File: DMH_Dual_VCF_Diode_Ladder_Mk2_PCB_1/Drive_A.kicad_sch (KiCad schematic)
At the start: 25 parts, among them J17 Conn_01x06_PinHeader, Q5 BC548, Q6 BC548, U9 TL074

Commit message: Added trim pot functions to silkscreen
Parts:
- RV26: Function (none) -> Drive A VCA Center
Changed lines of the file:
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@@
 		(on_board yes)
 		(dnp no)
-		(fields_autoplaced yes)
 		(property "Reference" "RV26"
 			(at 224.79 100.3299 0)
@@
 			)
 		)
+		(property "Function" "Drive A VCA Center"
+			(at 239.268 101.6 0)
+			(effects
+				(font
+					(size 1.27 1.27)
+					(thickness 0.254)
+					(bold yes)
+					(italic yes)
+				)
+			)
+		)

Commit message: Adjusted pin header connections
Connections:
- net Drive CV Input: now also J17.2 (Pin_2); no longer J17.1 (Pin_1)
- net at R113.1, RV27.2: now also J17.1 (Pin_1); no longer J17.3 (Pin_3)
- net at RV25.2, U9.12 (+): now also J17.3 (Pin_3); no longer J17.2 (Pin_2)
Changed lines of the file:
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@@
 		(lib_id "SynthStuff:Conn_01x06_PinHeader")
 		(at 63.5 81.28 270)
-		(unit 1)
+		(unit 2)
 		(exclude_from_sim no)
 		(in_bom yes)
@@
 				(path "/58f4306d-5387-4983-bb08-41a2313fd315/76f3ab41-888d-43b6-843a-2a995f9c890b"
 					(reference "J17")
-					(unit 1)
+					(unit 2)
 				)
 			)
@@
 		(lib_id "SynthStuff:Conn_01x06_PinHeader")
 		(at 76.2 100.33 90)
-		(unit 2)
+		(unit 3)
 		(exclude_from_sim no)
 		(in_bom yes)
@@
 				(path "/58f4306d-5387-4983-bb08-41a2313fd315/76f3ab41-888d-43b6-843a-2a995f9c890b"
 					(reference "J17")
-					(unit 2)
+					(unit 3)
 				)
 			)
@@
 		(lib_id "SynthStuff:Conn_01x06_PinHeader")
 		(at 110.49 129.54 90)
-		(unit 3)
+		(unit 1)
 		(exclude_from_sim no)
 		(in_bom yes)
@@
 				(path "/58f4306d-5387-4983-bb08-41a2313fd315/76f3ab41-888d-43b6-843a-2a995f9c890b"
 					(reference "J17")
-					(unit 3)
-				)
-			)
+					(unit 1)
+				)
+			)

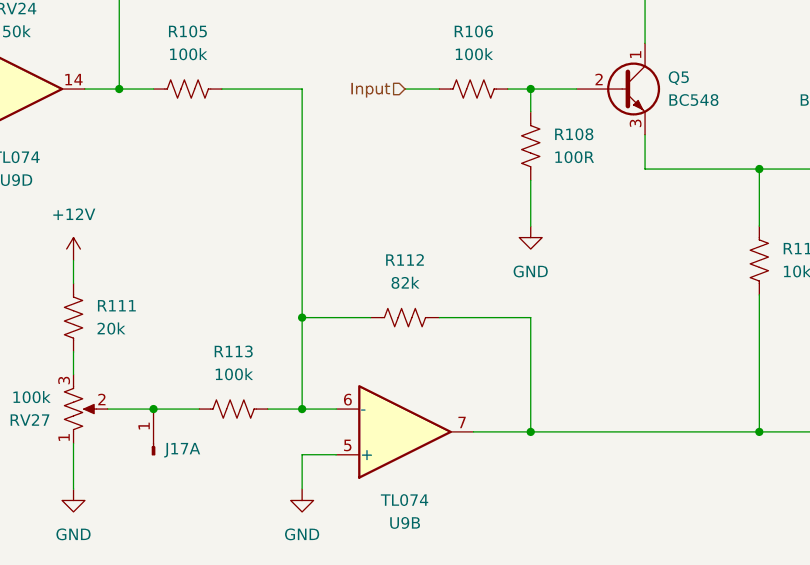
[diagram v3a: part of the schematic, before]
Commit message: Changed VCA CV summing stage feedback to 100k
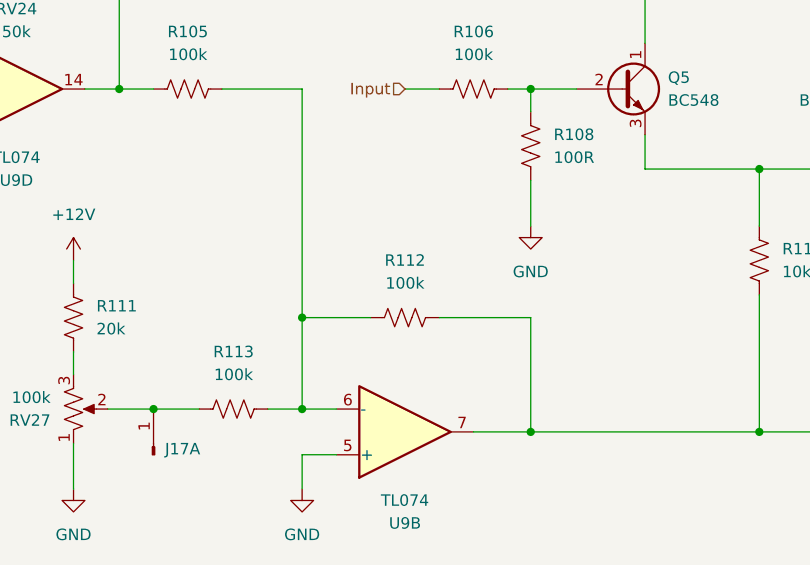
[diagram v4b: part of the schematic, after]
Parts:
- R112: value 82k -> 100k
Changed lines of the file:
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@@
 			)
 		)
-		(property "Value" "82k"
+		(property "Value" "100k"
 			(at 138.43 110.49 90)
 			(effects

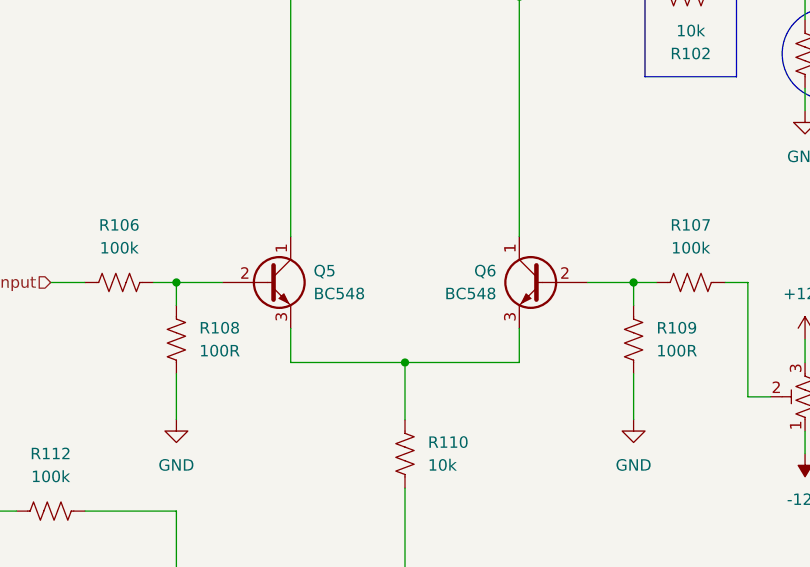
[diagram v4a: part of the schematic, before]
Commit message: Adding buffered input to CV3 - in progress
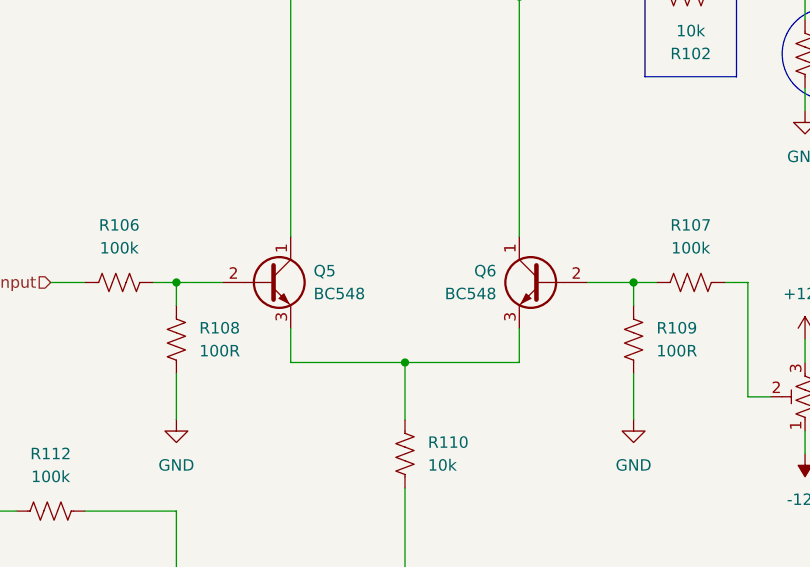
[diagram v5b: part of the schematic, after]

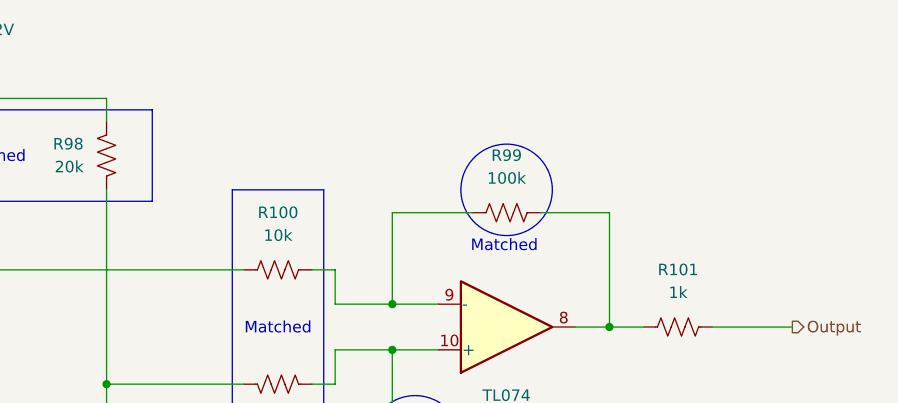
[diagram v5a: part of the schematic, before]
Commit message: Updated schematic during validation
- Changed Resonance B VCA gain resistors to 2k2
- Added range limiting resistors to all Cutoff pots
- Moved 48x gain to non-inverting opamp stage in Core Circuit to allow for Resonance voltage control.
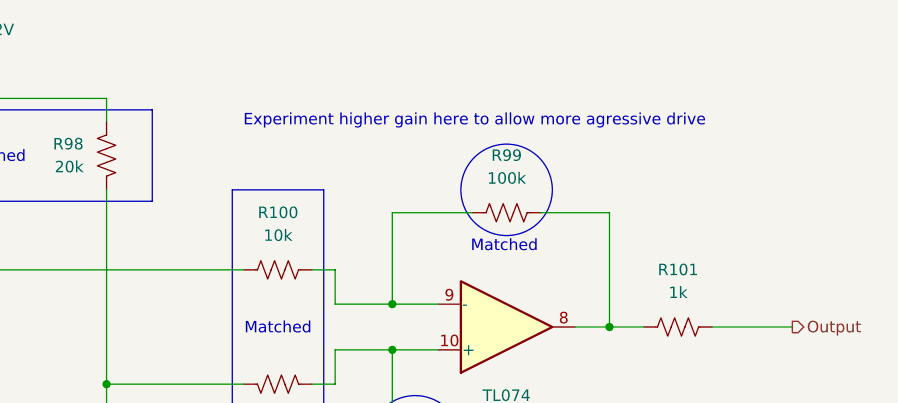
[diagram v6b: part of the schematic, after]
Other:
- note added: "Experiment higher gain here to allow more agressive drive"
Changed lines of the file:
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@@
+		)
+	)
+	(text "Experiment higher gain here to allow more agressive drive"
+		(exclude_from_sim no)
+		(at 231.394 27.94 0)
+		(effects
+			(font
+				(size 1.27 1.27)
+			)
 		)
 	)

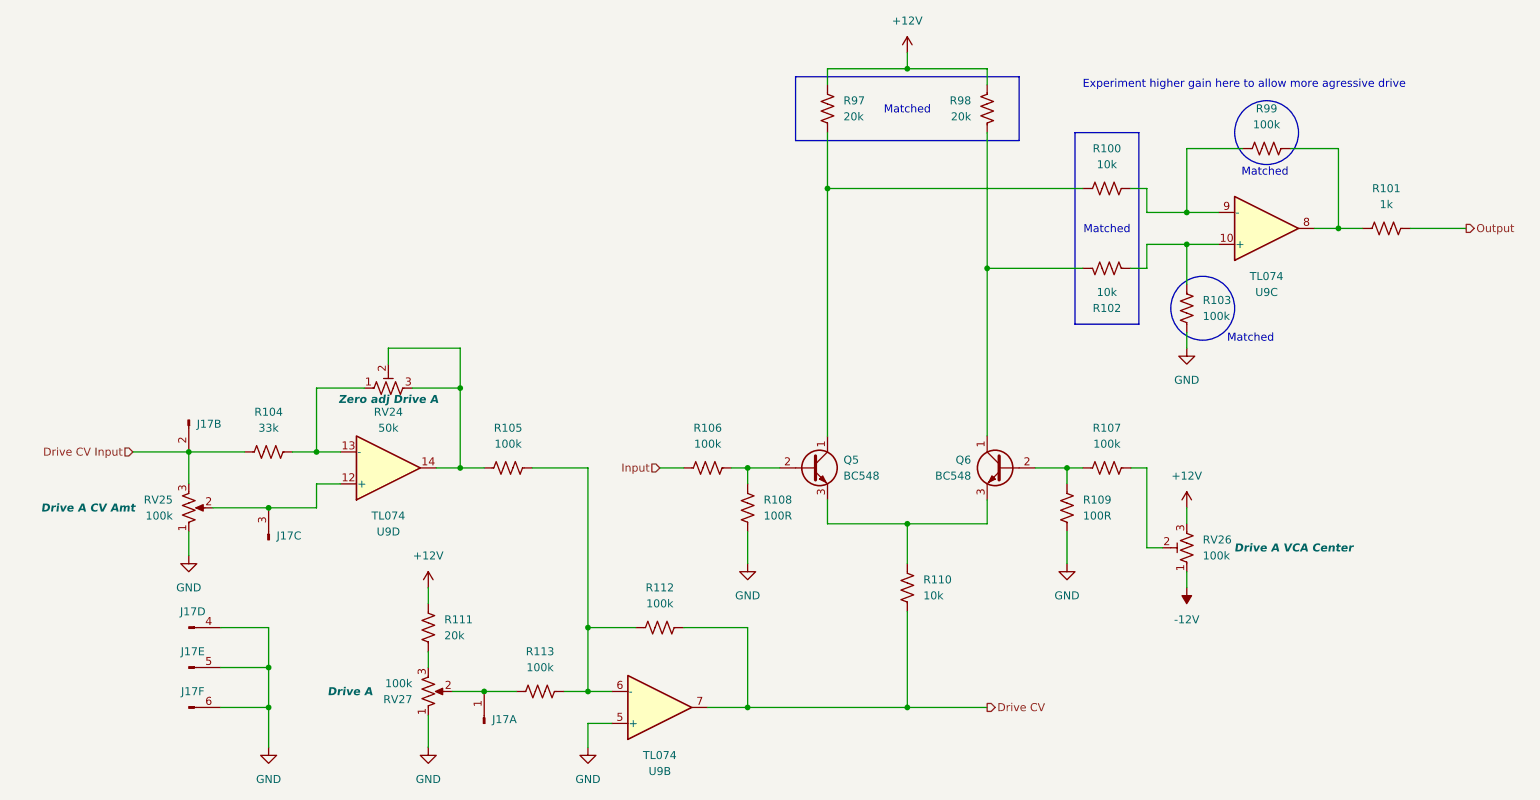
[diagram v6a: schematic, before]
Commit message: Updated various resistor values
... and deleted all VCAs output 1k resistors
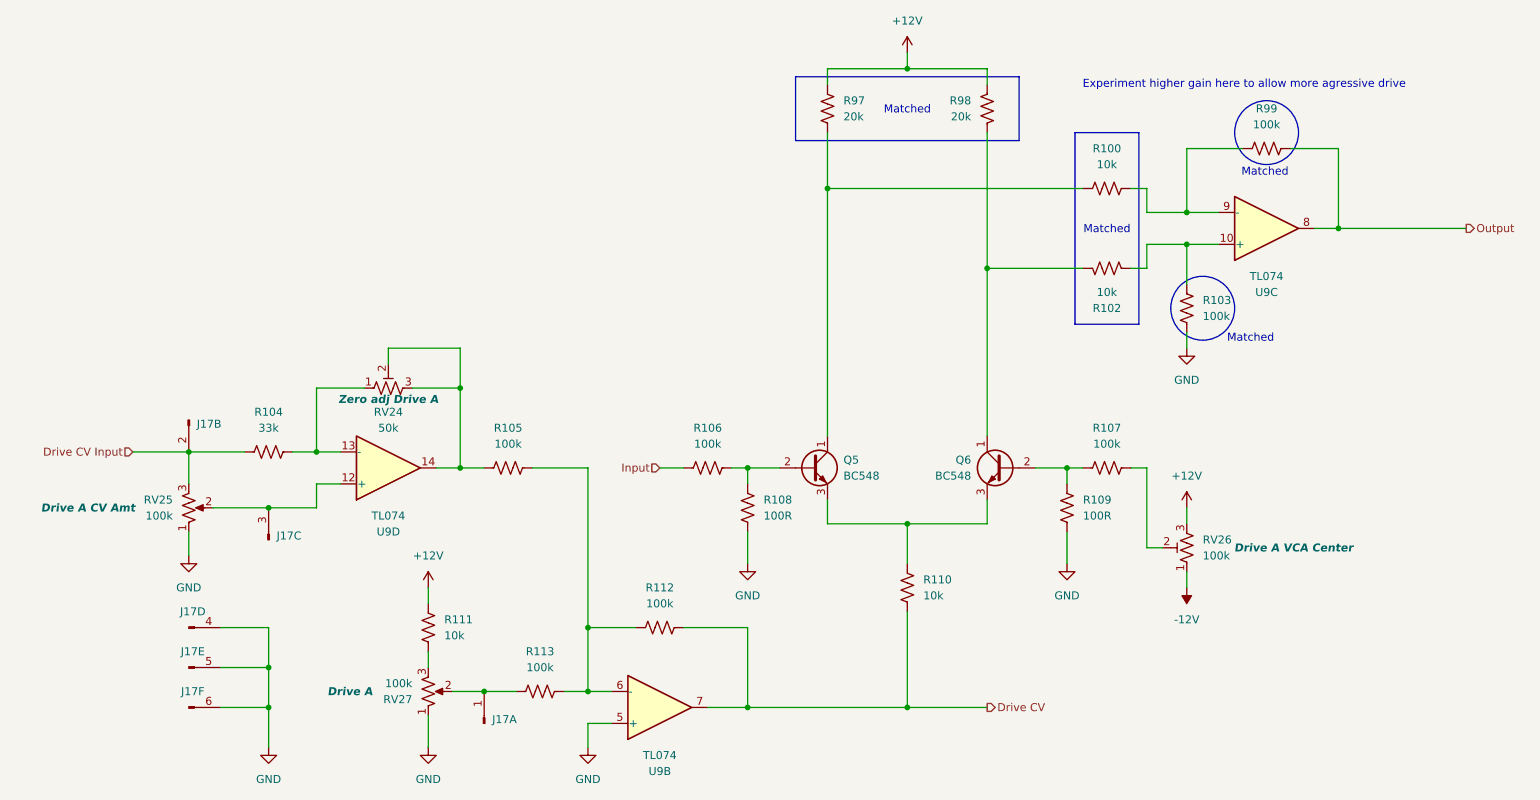
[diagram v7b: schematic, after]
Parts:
- removed R101: 1k, Resistor_THT:R_Axial_DIN0207_L6.3mm_D2.5mm_P7.62mm_Horizontal, symbol Device:R_US
- R111: value 20k -> 10k
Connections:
- net Output: now also R99.1, U9.8
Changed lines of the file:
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@@
 	(wire
 		(pts
-			(xy 257.81 50.8) (xy 266.7 50.8)
-		)
-		(stroke
-			(width 0)
-			(type default)
-		)
-	)
-	(wire
-		(pts
 			(xy 101.6 107.95) (xy 101.6 110.49)
 		)
@@
 	(wire
 		(pts
-			(xy 246.38 50.8) (xy 250.19 50.8)
+			(xy 246.38 50.8) (xy 266.7 50.8)
 		)
 		(stroke
@@
 	(symbol
 		(lib_id "Device:R_US")
-		(at 254 50.8 270)
-		(unit 1)
-		(exclude_from_sim no)
-		(in_bom yes)
-		(on_board yes)
-		(dnp no)
-		(fields_autoplaced yes)
-		(property "Reference" "R101"
-			(at 254 44.45 90)
-			(effects
-				(font
-					(size 1.27 1.27)
-				)
-			)
-		)
-		(property "Value" "1k"
-			(at 254 46.99 90)
-			(effects
-				(font
-					(size 1.27 1.27)
-				)
-			)
-		)
-		(property "Footprint" "Resistor_THT:R_Axial_DIN0207_L6.3mm_D2.5mm_P7.62mm_Horizontal"
-			(at 253.746 51.816 90)
-			(effects
-				(font
-					(size 1.27 1.27)
-				)
-				(hide yes)
-			)
-		)
-		(property "Datasheet" "~"
-			(at 254 50.8 0)
-			(effects
-				(font
-					(size 1.27 1.27)
-				)
-				(hide yes)
-			)
-		)
-		(property "Description" "Resistor, US symbol"
-			(at 254 50.8 0)
-			(effects
-				(font
-					(size 1.27 1.27)
-				)
-				(hide yes)
-			)
-		)
-		(property "Function" ""
-			(at 254 50.8 0)
-			(effects
-				(font
-					(size 1.27 1.27)
-				)
-			)
-		)
-		(pin "1"
-		)
-		(pin "2"
-		)
-		(instances
-			(project "DMH_Dual_VCF_Diode_Ladder_Mk2_PCB_1"
-				(path "/58f4306d-5387-4983-bb08-41a2313fd315/76f3ab41-888d-43b6-843a-2a995f9c890b"
-					(reference "R101")
-					(unit 1)
-				)
-			)
-		)
-	)
-	(symbol
-		(lib_id "Device:R_US")
 		(at 209.55 88.9 270)
 		(unit 1)
@@
 			)
 		)
-		(property "Value" "20k"
+		(property "Value" "10k"
 			(at 104.14 115.5699 0)
 			(effects

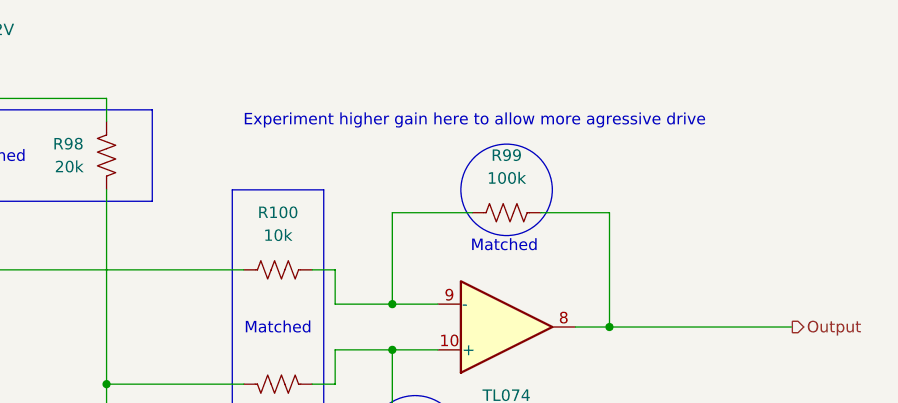
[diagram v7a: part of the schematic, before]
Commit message: Synchronized changes from PCB 1 to PCB 2 schematic
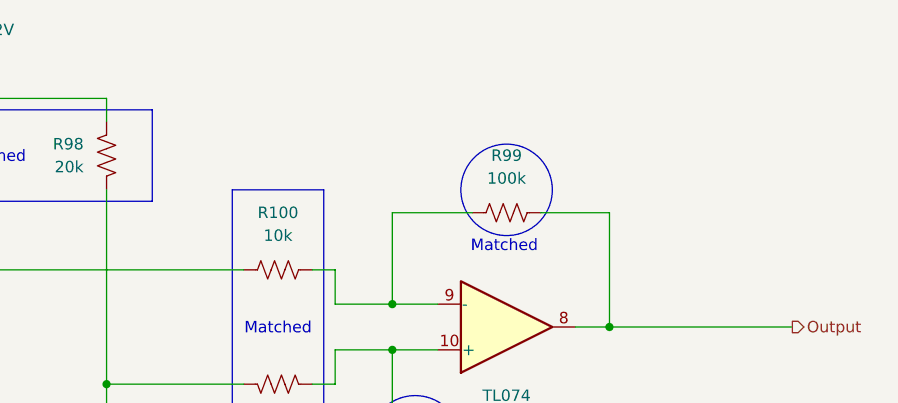
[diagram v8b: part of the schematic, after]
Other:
- note removed: "Experiment higher gain here to allow more agressive drive"
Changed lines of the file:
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@@
-		)
-	)
-	(text "Experiment higher gain here to allow more agressive drive"
-		(exclude_from_sim no)
-		(at 231.394 27.94 0)
-		(effects
-			(font
-				(size 1.27 1.27)
-			)
 		)
 	)
